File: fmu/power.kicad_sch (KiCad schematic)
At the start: 35 parts, among them J1 1054500101, U1 MAX77960BEFV12+, U10 DMN3016LK3-13, U11 BQ7694203PFBR, U9 MAX20075ATCA/V+

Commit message: Add voltage regulators
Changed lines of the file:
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@@
 	)
 	(junction
+		(at 104.14 152.4)
+		(diameter 0)
+		(color 0 0 0 0)
+	)
+	(junction
 		(at 137.16 113.03)
 		(diameter 0)
@@
 	(wire
 		(pts
-			(xy 104.14 151.13) (xy 104.14 154.94)
+			(xy 104.14 151.13) (xy 104.14 152.4)
 		)
 		(stroke
@@
 	(wire
 		(pts
+			(xy 104.14 152.4) (xy 104.14 154.94)
+		)
+		(stroke
+			(width 0)
+			(type default)
+		)
+	)
+	(wire
+		(pts
 			(xy 19.05 63.5) (xy 19.05 66.04)
 		)
@@
 					(unit 1)
 				)
+			)
+		)
+	)
+	(symbol
+		(lib_id "power:PWR_FLAG")
+		(at 104.14 152.4 270)
+		(unit 1)
+		(exclude_from_sim no)
+		(in_bom yes)
+		(on_board yes)
+		(dnp no)
+		(fields_autoplaced yes)
+		(property "Reference" "#FLG04"
+			(at 106.045 152.4 0)
+			(effects
+				(font
+					(size 1.27 1.27)
+				)
+				(hide yes)
+			)
+		)
+		(property "Value" "PWR_FLAG"
+			(at 107.95 152.3999 90)
+			(effects
+				(font
+					(size 1.27 1.27)
+				)
+				(justify left)
+			)
+		)
+		(property "Footprint" ""
+			(at 104.14 152.4 0)
+			(effects
+				(font
+					(size 1.27 1.27)
+				)
+				(hide yes)
+			)
+		)
+		(property "Datasheet" "~"
+			(at 104.14 152.4 0)
+			(effects
+				(font
+					(size 1.27 1.27)
+				)
+				(hide yes)
+			)
+		)
+		(property "Description" "Special symbol for telling ERC where power comes from"
+			(at 104.14 152.4 0)
+			(effects
+				(font
+					(size 1.27 1.27)
+				)
+				(hide yes)
+			)
+		)
+		(pin "1"
+		)
+		(instances
+			(project "fmu"
+				(path "/4752d952-9322-46fb-9cc2-2404eb91f5a4/ea2647fd-fd97-4607-acae-2a9c5eb57707"
+					(reference "#FLG04")
+					(unit 1)
+				)

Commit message: Fix some connections
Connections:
- net BATT is gone; now on net +12V: CC9.2, D1.2 (A), RC7.1, U1.11 (BATSP), U1.12 (BATT)
- net BATTN is gone; now on net GND: CC13.1, RC9.2, U10.3 (S)
- net PACK_NEG is gone; now on net GND: CELL1.2 (-), U11.16 (VC0)
- net INTB: no longer names the net of U1.18 (INTB)
- no-connect marks 7 -> 10
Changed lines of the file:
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@@
 	)
 	(junction
+		(at 81.28 186.69)
+		(diameter 0)
+		(color 0 0 0 0)
+	)
+	(junction
 		(at 153.67 119.38)
 		(diameter 0)
@@
 	)
 	(junction
+		(at 104.14 191.77)
+		(diameter 0)
+		(color 0 0 0 0)
+	)
+	(junction
 		(at 24.13 100.33)
 		(diameter 0)
@@
 	)
 	(junction
+		(at 44.45 140.97)
+		(diameter 0)
+		(color 0 0 0 0)
+	)
+	(junction
 		(at 137.16 115.57)
 		(diameter 0)
@@
 	)
 	(no_connect
+		(at 85.09 130.81)
+	)
+	(no_connect
+		(at 85.09 133.35)
+	)
+	(no_connect
+		(at 138.43 128.27)
+	)
+	(no_connect
 		(at 213.36 66.04)
 	)
@@
 	(wire
 		(pts
-			(xy 83.82 186.69) (xy 78.74 186.69)
+			(xy 83.82 186.69) (xy 81.28 186.69)
 		)
 		(stroke
@@
 	(wire
 		(pts
+			(xy 57.15 140.97) (xy 44.45 140.97)
+		)
+		(stroke
+			(width 0)
+			(type default)
+		)
+	)
+	(wire
+		(pts
 			(xy 171.45 107.95) (xy 173.99 107.95)
 		)
@@
 	(wire
 		(pts
+			(xy 102.87 191.77) (xy 104.14 191.77)
+		)
+		(stroke
+			(width 0)
+			(type default)
+		)
+	)
+	(wire
+		(pts
 			(xy 44.45 142.24) (xy 44.45 144.78)
 		)
@@
 	(wire
 		(pts
+			(xy 81.28 190.5) (xy 81.28 186.69)
+		)
+		(stroke
+			(width 0)
+			(type default)
+		)
+	)
+	(wire
+		(pts
 			(xy 35.56 100.33) (xy 39.37 100.33)
 		)
@@
 	(wire
 		(pts
+			(xy 81.28 186.69) (xy 78.74 186.69)
+		)
+		(stroke
+			(width 0)
+			(type default)
+		)
+	)
+	(wire
+		(pts
 			(xy 135.89 123.19) (xy 137.16 123.19)
 		)
@@
 	(wire
 		(pts
+			(xy 44.45 140.97) (xy 44.45 142.24)
+		)
+		(stroke
+			(width 0)
+			(type default)
+		)
+	)
+	(wire
+		(pts
 			(xy 39.37 114.3) (xy 39.37 109.22)
 		)
@@
 	(wire
 		(pts
-			(xy 44.45 139.7) (xy 44.45 142.24)
+			(xy 83.82 190.5) (xy 81.28 190.5)
+		)
+		(stroke
+			(width 0)
+			(type default)
+		)
+	)
+	(wire
+		(pts
+			(xy 44.45 139.7) (xy 44.45 140.97)
 		)
 		(stroke
@@
 	)
 	(rectangle
+		(start 55.88 137.16)
+		(end 68.58 142.24)
+		(stroke
+			(width 0)
+			(type default)
+		)
+		(fill
+			(type none)
+		)
+	)
+	(rectangle
+		(start 196.85 71.12)
+		(end 208.28 82.55)
+		(stroke
+			(width 0)
+			(type default)
+		)
+		(fill
+			(type none)
+		)
+	)
+	(rectangle
 		(start 102.87 143.51)
 		(end 114.3 147.32)
@@
 	)
 	(rectangle
+		(start 83.82 187.96)
+		(end 93.98 191.77)
+		(stroke
+			(width 0)
+			(type default)
+		)
+		(fill
+			(type none)
+		)
+	)
+	(rectangle
 		(start 97.79 147.32)
 		(end 119.38 195.58)
@@
 		)
 	)
-	(text_box "3S 11V battery pack\n\nNotes: Connect BATT and BATTN"
+	(text_box "3S 11V battery pack\n"
 		(exclude_from_sim no)
 		(at 123.19 179.07 0)
-		(size 22.86 10.16)
+		(size 22.86 3.81)
 		(stroke
 			(width 0)
@@
 		)
 	)
+	(label "PACK_NEG"
+		(at 83.82 190.5 0)
+		(fields_autoplaced yes)
+		(effects
+			(font
+				(size 1.27 1.27)
+			)
+			(justify left bottom)
+		)
+	)
 	(label "BATTSN"
 		(at 69.85 189.23 0)
@@
 		)
 	)
+	(label "PACK_POS"
+		(at 57.15 140.97 0)
+		(fields_autoplaced yes)
+		(effects
+			(font
+				(size 1.27 1.27)
+			)
+			(justify left bottom)
+		)
+	)
 	(label "VPVL"
 		(at 146.05 143.51 0)
@@
 		)
 	)
-	(hierarchical_label "INTB"
-		(shape input)
-		(at 138.43 128.27 0)
-		(fields_autoplaced yes)
-		(effects
-			(font
-				(size 1.27 1.27)
-			)
-			(justify left)
-		)
-	)
 	(symbol
 		(lib_id "power:GND")
@@
 					(unit 1)
 				)
+			)
+		)
+	)
+	(symbol
+		(lib_id "power:GND")
+		(at 102.87 191.77 0)
+		(unit 1)
+		(exclude_from_sim no)
+		(in_bom yes)
+		(on_board yes)
+		(dnp no)
+		(fields_autoplaced yes)
+		(property "Reference" "#PWR0129"
+			(at 102.87 198.12 0)
+			(effects
+				(font
+					(size 1.27 1.27)
+				)
+				(hide yes)
+			)
+		)
+		(property "Value" "GND"
+			(at 102.87 196.85 0)
+			(effects
+				(font
+					(size 1.27 1.27)
+				)
+				(hide yes)
+			)
+		)
+		(property "Footprint" ""
+			(at 102.87 191.77 0)
+			(effects
+				(font
+					(size 1.27 1.27)
+				)
+				(hide yes)
+			)
+		)
+		(property "Datasheet" ""
+			(at 102.87 191.77 0)
+			(effects
+				(font
+					(size 1.27 1.27)
+				)
+				(hide yes)
+			)
+		)
+		(property "Description" "Power symbol creates a global label with name \"GND\" , ground"
+			(at 102.87 191.77 0)
+			(effects
+				(font
+					(size 1.27 1.27)
+				)
+				(hide yes)
+			)
+		)
+		(pin "1"
+		)
+		(instances
+			(project "fmu"
+				(path "/4752d952-9322-46fb-9cc2-2404eb91f5a4/ea2647fd-fd97-4607-acae-2a9c5eb57707"
+					(reference "#PWR0129")
+					(unit 1)
+				)

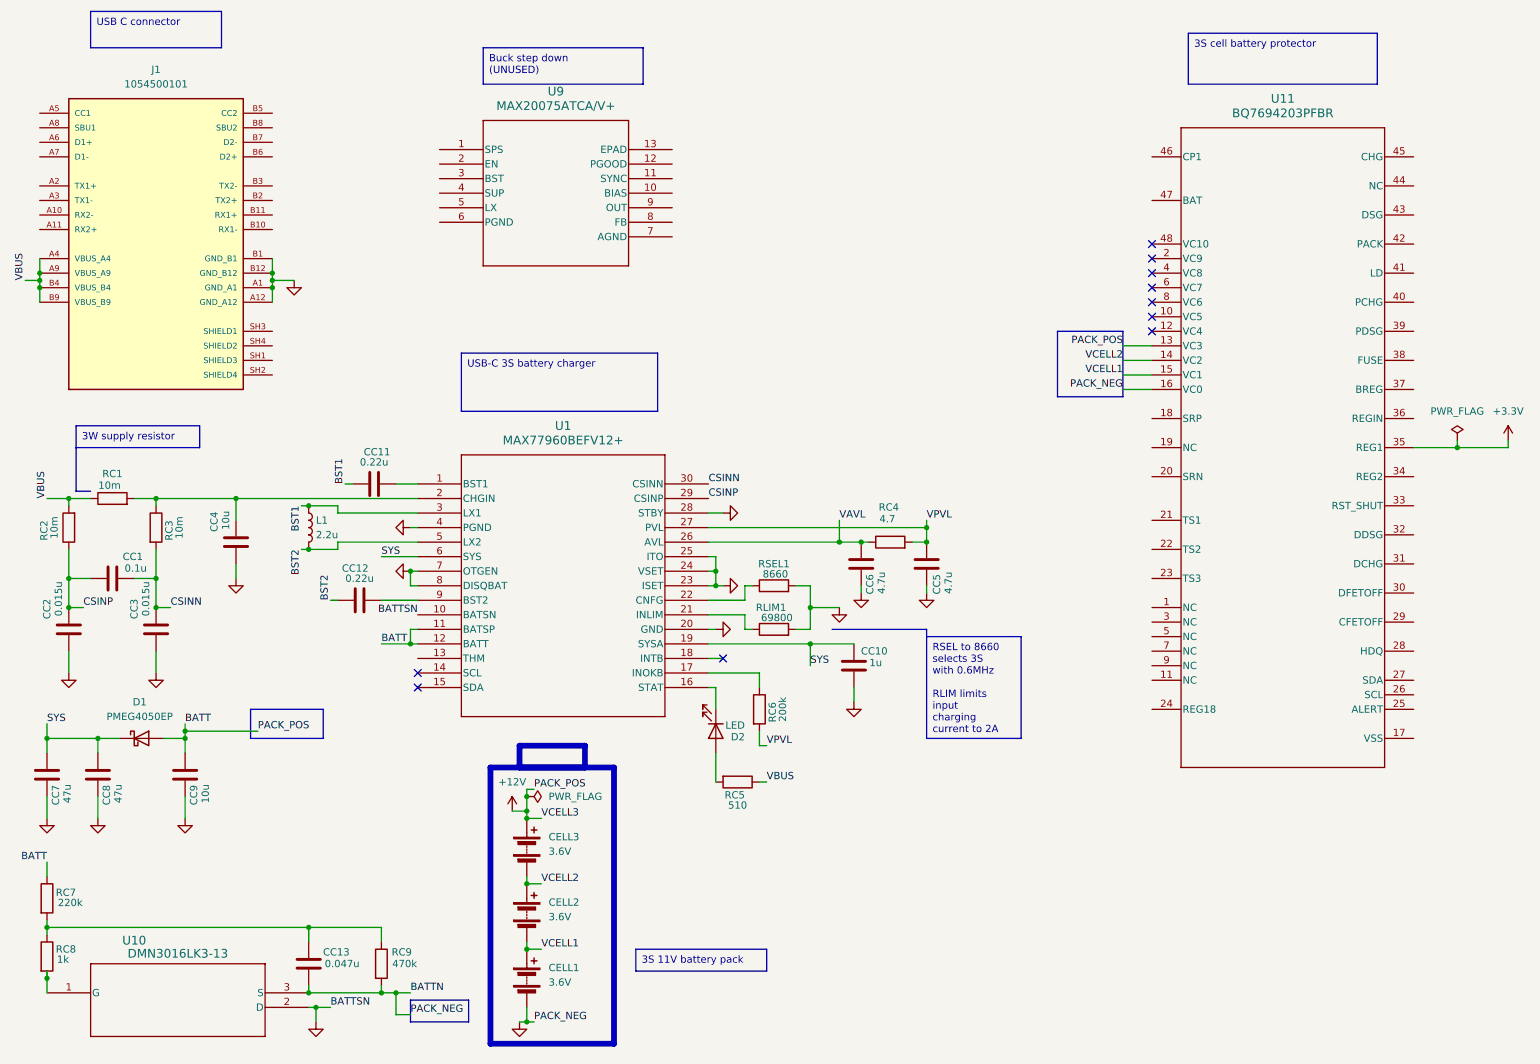
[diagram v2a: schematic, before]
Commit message: Implement battery charger
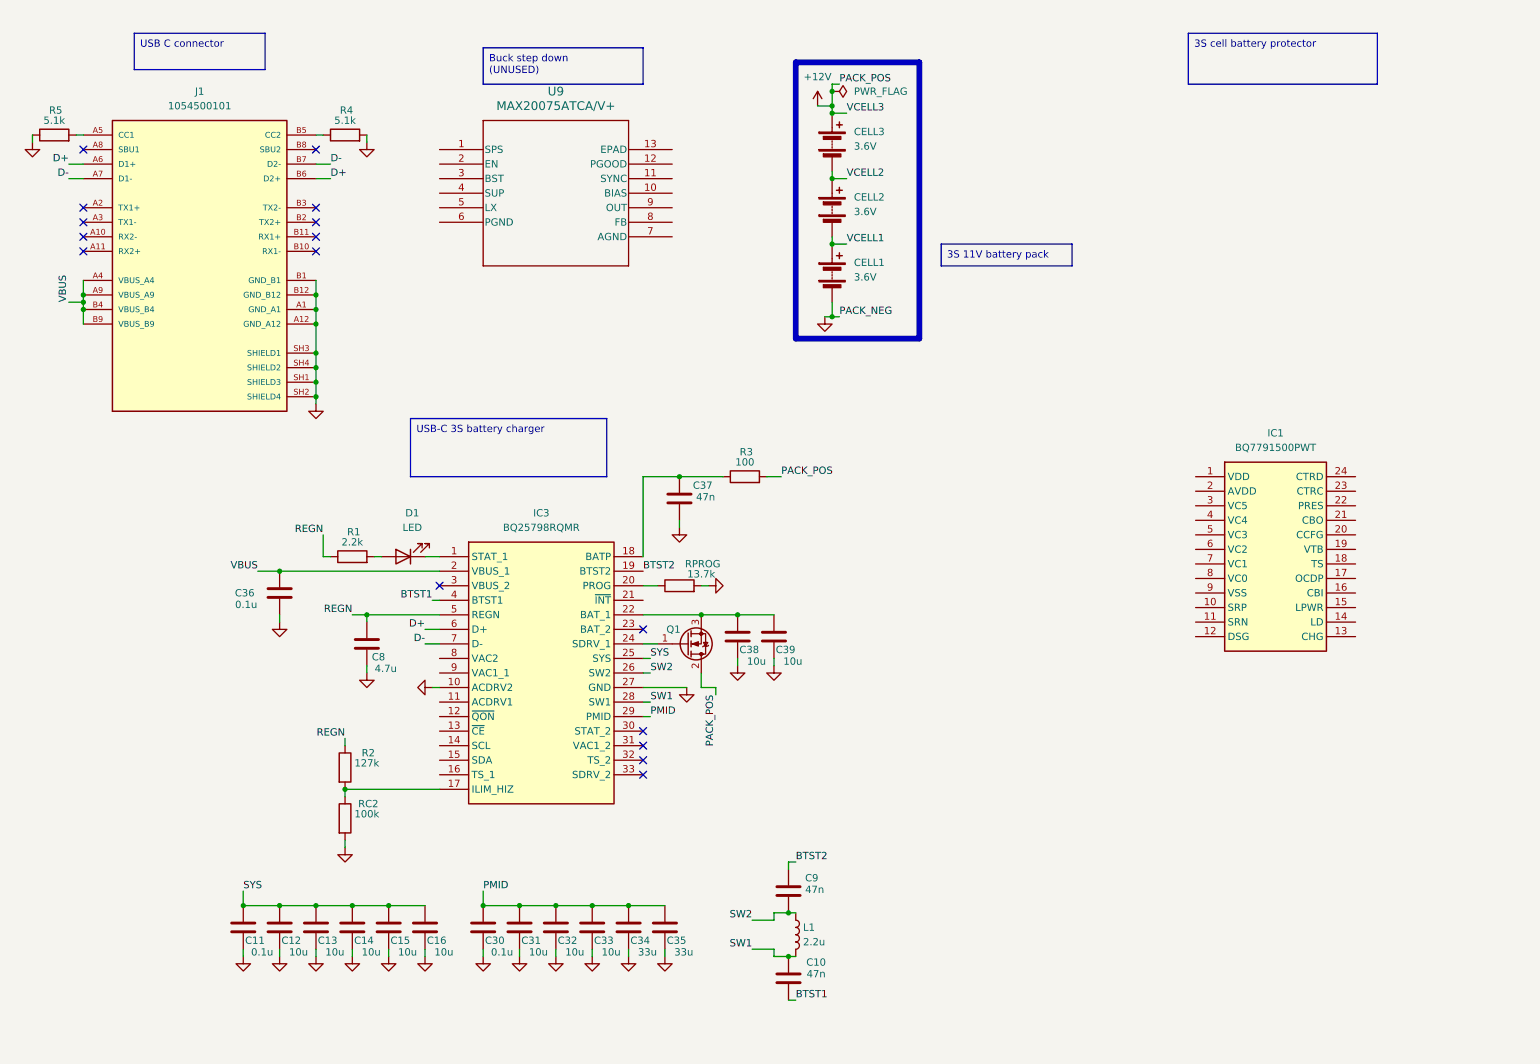
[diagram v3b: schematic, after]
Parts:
- removed CC1: 0.1u, Capacitor_SMD:C_0603_1608Metric, symbol Device:C
- removed CC10: 1u, Capacitor_SMD:C_0603_1608Metric, symbol Device:C
- removed CC11, CC12: 0.22u, Capacitor_SMD:C_0603_1608Metric, symbol Device:C
- removed CC13: 0.047u, Capacitor_SMD:C_0603_1608Metric, symbol Device:C
- removed CC2, CC3: 0.015u, Capacitor_SMD:C_0603_1608Metric, symbol Device:C
- removed CC4, CC9: 10u, Capacitor_SMD:C_0603_1608Metric, symbol Device:C
- removed CC5, CC6: 4.7u, Capacitor_SMD:C_0603_1608Metric, symbol Device:C
- removed CC7, CC8: 47u, Capacitor_SMD:C_0603_1608Metric, symbol Device:C
- removed D1: PMEG4050EP, Diode_SMD:D_SOD-128, symbol Diode:PMEG4050EP
- removed D2: LED, LED_SMD:LED_0603_1608Metric, symbol Device:LED
- removed RC1, RC3: 10m, Resistor_SMD:R_0603_1608Metric, symbol Device:R
- removed RC4: 4.7, Resistor_SMD:R_0603_1608Metric, symbol Device:R
- removed RC5: 510, Resistor_SMD:R_0603_1608Metric, symbol Device:R
- removed RC6: 200k, Resistor_SMD:R_0603_1608Metric, symbol Device:R
- removed RC7: 220k, Resistor_SMD:R_0603_1608Metric, symbol Device:R
- removed RC8: 1k, Resistor_SMD:R_0603_1608Metric, symbol Device:R
- removed RC9: 470k, Resistor_SMD:R_0603_1608Metric, symbol Device:R
- removed RLIM1: 69800, Resistor_SMD:R_0603_1608Metric, symbol Device:R
- removed RSEL1: 8660, Resistor_SMD:R_0603_1608Metric, symbol Device:R
- removed U1: MAX77960BEFV12+, 90-100100_F304A4F+1_MXM, symbol 2024-03-25_18-47-05:MAX77960BEFV12+
- removed U10: DMN3016LK3-13, TO-252_DIO, symbol 2024-03-27_22-02-08:DMN3016LK3-13
- removed U11: BQ7694203PFBR, PFB0048A_N, symbol 2024-04-05_13-24-07:BQ7694203PFBR
- added C10, C37, C9: 47n, Capacitor_SMD:C_0603_1608Metric, symbol Device:C
- added C11, C30, C36: 0.1u, Capacitor_SMD:C_0603_1608Metric, symbol Device:C
- added C12, C13, C14, C15, C16, C31, C32, C33, C38, C39: 10u, Capacitor_SMD:C_0603_1608Metric, symbol Device:C
- added C34, C35: 33u, Capacitor_SMD:C_0603_1608Metric, symbol Device:C
- added C8: 4.7u, Capacitor_SMD:C_0603_1608Metric, symbol Device:C
- added D1: LED, LED_SMD:LED_0603_1608Metric, symbol Device:LED
- added IC1: BQ7791500PWT, SOP65P640X120-24N, symbol BQ7791500PWT:BQ7791500PWT
- added IC3: BQ25798RQMR, BQ25798RQMR, symbol BQ25798RQMR:BQ25798RQMR
- added Q1: NDT3055L, Package_TO_SOT_SMD:SOT-223-3_TabPin2, symbol Transistor_FET:NDT3055L
- added R1: 2.2k, Resistor_SMD:R_0603_1608Metric, symbol Device:R
- added R2: 127k, Resistor_SMD:R_0603_1608Metric, symbol Device:R
- added R3: 100, Resistor_SMD:R_0603_1608Metric, symbol Device:R
- added R4, R5: 5.1k, Resistor_SMD:R_0603_1608Metric, symbol Device:R
- added RPROG: 13.7k, Resistor_SMD:R_0603_1608Metric, symbol Device:R
- L1: Sat Current 8A -> (none)
- RC2: value 10m -> 100k
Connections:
- net +12V: now also Q1.2 (D), R3.2
- net GND: now also J1.SH1 (SHIELD3), J1.SH2 (SHIELD4), J1.SH3 (SHIELD1), J1.SH4 (SHIELD2), RC2.2, C11.1, C12.1, C13.1, C14.1, C15.1, C16.1, C30.1, C31.1, C32.1, C33.1, C34.1, C35.1, C36.1, C37.1, C38.1, C39.1, C8.1, IC3.10 (ACDRV2), IC3.27 (GND), R4.2, R5.1, RPROG.2
- net SYS: now also C11.2, C12.2, C13.2, C14.2, C15.2, C16.2, IC3.25 (SYS)
- net VBUS: now also C36.2, IC3.2 (VBUS_1); no longer RC2.2
- net at J1.A5 (CC1): now also R5.2
- net D+: now reaches J1.A6 (D1+)
- net D+: now also J1.B6 (D2+), IC3.6 (D+)
- net D-: now reaches J1.A7 (D1-)
- net D-: now also J1.B7 (D2-), IC3.7 (D-)
- net at J1.B5 (CC2): now also R4.1
- net BST1 renamed SW2
- net SW2: now also C9.1, IC3.26 (SW2)
- net BST2 renamed SW1
- net SW1: now also C10.2, IC3.28 (SW1)
- net CSINP: no longer names the net of RC2.1
- net CSINP: now also IC3.17 (ILIM_HIZ), R2.2
- new net: C38.2, C39.2, IC3.22 (BAT_1), Q1.3 (S)
- new net: C37.2, IC3.18 (BATP), R3.1
- new net: IC3.24 (SDRV_1), Q1.1 (G)
- new net: D1.2 (A), R1.2
- new net: D1.1 (K), IC3.1 (STAT_1)
- new net: IC3.20 (PROG), RPROG.1
- new net BTST1: C10.1, IC3.4 (BTST1)
- new net BTST2: C9.2, IC3.19 (BTST2)
- new net PMID: C30.2, C31.2, C32.2, C33.2, C34.2, C35.2, IC3.29 (PMID)
- new net REGN: C8.2, IC3.5 (REGN), R1.1, R2.1
- no-connect marks 10 -> 16
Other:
- moved on the sheet: CELL1, CELL2, CELL3, J1

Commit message: Start wiring battery protector; mark charger as non-BOM
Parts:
- added CIN1, CIN2, CIN3, CIN4: 0.1u, Capacitor_SMD:C_0603_1608Metric, symbol Device:C
- added CIN5: 1u, Capacitor_SMD:C_0603_1608Metric, symbol Device:C
- added Q2: NDT3055L, Package_TO_SOT_SMD:SOT-223-3_TabPin2, symbol Transistor_FET:NDT3055L
- added RLD: 450k, Resistor_SMD:R_0603_1608Metric, symbol Device:R
- added ROCD: 100k, Resistor_SMD:R_0603_1608Metric, symbol Device:R
- added RSENS1, RSENS2, RSENS3, RSENS4, RVDD: 1k, Resistor_SMD:R_0603_1608Metric, symbol Device:R
- renumbered RPROG to RPROG1
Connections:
- net +12V: now also RSENS3.1
- net GND: now also IC1.16 (CBI), IC1.23 (CTRC), IC1.24 (CTRD), IC1.9 (VSS), CIN3.2, CIN4.2, CIN5.1, ROCD.2; no longer CELL1.2 (-)
- net VCELL1: now also RSENS1.1
- net VCELL2: now also RSENS2.1
- net at IC1.1 (VDD): now also RVDD.2
- net at IC1.14 (LD): now also RLD.1
- net at IC1.17 (OCDP): now also ROCD.1
- net at IC1.2 (AVDD): now also CIN5.2
- net at IC1.3 (VC5): now also IC1.4 (VC4), IC1.5 (VC3), CIN2.2, RSENS3.2, RVDD.1
- net at IC1.6 (VC2): now also CIN1.2, CIN2.1, RSENS2.2
- net at IC1.7 (VC1): now also CIN1.1, CIN3.1, RSENS1.2
- net at IC1.8 (VC0): now also CIN4.1, RSENS4.2
- new net PACK_NEG: CELL1.2 (-), RLD.2, RSENS4.1
- no-connect marks 16 -> 19
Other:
- moved on the sheet: C10, C11, C12, C13, C14, C15, C16, C30, C31, C32, C33, C34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
